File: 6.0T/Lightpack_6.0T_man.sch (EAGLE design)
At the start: 31 parts, among them CN1 USB-MICRO-B, CN2 RJ11-5P-REEL-LIGHTPACK6T2, CN3 RJ11-5P-REEL-MAIN, IC1 AT90USB162, IC2 DM631_SOP24, IC3 DM631_SOP24, J1 DCJ0202, X1 16Mhz

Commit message: New universal microUSB footprint
*Some restriction added
*7 holes on milling (46) layer
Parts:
- CN1: value USB-MICRO-B -> USB-MICRO-B-UNIVERSAL; device _USB_sockets:USB-MICRO-B -> _USB_sockets:USB-MICRO-B-UNIVERSAL
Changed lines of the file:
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@@
 <grid distance="0.1" unitdist="inch" unit="inch" style="lines" multiple="1" display="no" altdistance="0.01" altunitdist="inch" altunit="inch"/>
 <layers>
-<layer number="1" name="Top" color="4" fill="1" visible="no" active="no"/>
-<layer number="2" name="Route2" color="1" fill="3" visible="no" active="no"/>
-<layer number="15" name="Route15" color="4" fill="6" visible="no" active="no"/>
-<layer number="16" name="Bottom" color="1" fill="1" visible="no" active="no"/>
-<layer number="17" name="Pads" color="2" fill="1" visible="no" active="no"/>
-<layer number="18" name="Vias" color="2" fill="1" visible="no" active="no"/>
-<layer number="19" name="Unrouted" color="6" fill="1" visible="no" active="no"/>
-<layer number="20" name="Dimension" color="15" fill="1" visible="no" active="no"/>
-<layer number="21" name="tPlace" color="14" fill="1" visible="no" active="no"/>
-<layer number="22" name="bPlace" color="7" fill="1" visible="no" active="no"/>
-<layer number="23" name="tOrigins" color="15" fill="1" visible="no" active="no"/>
-<layer number="24" name="bOrigins" color="15" fill="1" visible="no" active="no"/>
-<layer number="25" name="tNames" color="7" fill="1" visible="no" active="no"/>
-<layer number="26" name="bNames" color="7" fill="1" visible="no" active="no"/>
-<layer number="27" name="tValues" color="7" fill="1" visible="no" active="no"/>
-<layer number="28" name="bValues" color="7" fill="1" visible="no" active="no"/>
+<layer number="1" name="Top" color="4" fill="1" visible="yes" active="no"/>
+<layer number="2" name="Route2" color="1" fill="3" visible="yes" active="no"/>
+<layer number="15" name="Route15" color="4" fill="6" visible="yes" active="no"/>
+<layer number="16" name="Bottom" color="1" fill="1" visible="yes" active="no"/>
+<layer number="17" name="Pads" color="2" fill="1" visible="yes" active="no"/>
+<layer number="18" name="Vias" color="2" fill="1" visible="yes" active="no"/>
+<layer number="19" name="Unrouted" color="6" fill="1" visible="yes" active="no"/>
+<layer number="20" name="Dimension" color="15" fill="1" visible="yes" active="no"/>
+<layer number="21" name="tPlace" color="14" fill="1" visible="yes" active="no"/>
+<layer number="22" name="bPlace" color="7" fill="1" visible="yes" active="no"/>
+<layer number="23" name="tOrigins" color="15" fill="1" visible="yes" active="no"/>
+<layer number="24" name="bOrigins" color="15" fill="1" visible="yes" active="no"/>
+<layer number="25" name="tNames" color="7" fill="1" visible="yes" active="no"/>
+<layer number="26" name="bNames" color="7" fill="1" visible="yes" active="no"/>
+<layer number="27" name="tValues" color="7" fill="1" visible="yes" active="no"/>
+<layer number="28" name="bValues" color="7" fill="1" visible="yes" active="no"/>
 <layer number="29" name="tStop" color="7" fill="3" visible="no" active="no"/>
 <layer number="30" name="bStop" color="7" fill="6" visible="no" active="no"/>
@@
 <layer number="35" name="tGlue" color="7" fill="4" visible="no" active="no"/>
 <layer number="36" name="bGlue" color="7" fill="5" visible="no" active="no"/>
-<layer number="37" name="tTest" color="7" fill="1" visible="no" active="no"/>
-<layer number="38" name="bTest" color="7" fill="1" visible="no" active="no"/>
+<layer number="37" name="tTest" color="7" fill="1" visible="yes" active="no"/>
+<layer number="38" name="bTest" color="7" fill="1" visible="yes" active="no"/>
 <layer number="39" name="tKeepout" color="4" fill="11" visible="no" active="no"/>
 <layer number="40" name="bKeepout" color="1" fill="11" visible="no" active="no"/>
@@
 <layer number="44" name="Drills" color="7" fill="1" visible="no" active="no"/>
 <layer number="45" name="Holes" color="7" fill="1" visible="no" active="no"/>
-<layer number="46" name="Milling" color="3" fill="1" visible="no" active="no"/>
-<layer number="47" name="Measures" color="7" fill="1" visible="no" active="no"/>
-<layer number="48" name="Document" color="7" fill="1" visible="no" active="no"/>
-<layer number="49" name="Reference" color="7" fill="1" visible="no" active="no"/>
-<layer number="50" name="dxf" color="7" fill="1" visible="no" active="no"/>
-<layer number="51" name="tDocu" color="7" fill="1" visible="no" active="no"/>
-<layer number="52" name="bDocu" color="7" fill="1" visible="no" active="no"/>
-<layer number="53" name="tGND_GNDA" color="7" fill="9" visible="no" active="no"/>
-<layer number="54" name="bGND_GNDA" color="1" fill="9" visible="no" active="no"/>
-<layer number="56" name="wert" color="7" fill="1" visible="no" active="no"/>
+<layer number="46" name="Milling" color="3" fill="1" visible="yes" active="no"/>
+<layer number="47" name="Measures" color="7" fill="1" visible="yes" active="no"/>
+<layer number="48" name="Document" color="7" fill="1" visible="yes" active="no"/>
+<layer number="49" name="Reference" color="7" fill="1" visible="yes" active="no"/>
+<layer number="50" name="dxf" color="7" fill="1" visible="yes" active="no"/>
+<layer number="51" name="tDocu" color="7" fill="1" visible="yes" active="no"/>
+<layer number="52" name="bDocu" color="7" fill="1" visible="yes" active="no"/>
+<layer number="53" name="tGND_GNDA" color="7" fill="9" visible="yes" active="no"/>
+<layer number="54" name="bGND_GNDA" color="1" fill="9" visible="yes" active="no"/>
+<layer number="56" name="wert" color="7" fill="1" visible="yes" active="no"/>
 <layer number="91" name="Nets" color="2" fill="1" visible="yes" active="yes"/>
 <layer number="92" name="Busses" color="1" fill="1" visible="yes" active="yes"/>
@@
 <part name="GND11" library="supply1" deviceset="GND" device=""/>
 <part name="FRAME2" library="frames" deviceset="A4L-LOC" device="" value="Lightpack"/>
-<part name="CN1" library="_USB_sockets" deviceset="USB-MICRO-B" device=""/>
+<part name="CN1" library="_USB_sockets" deviceset="USB-MICRO-B" device="-UNIVERSAL"/>
 <part name="GND13" library="supply1" deviceset="GND" device=""/>
 <part name="C6" library="rcl" deviceset="C-EU" device="C0805" value="10nF/500V"/>

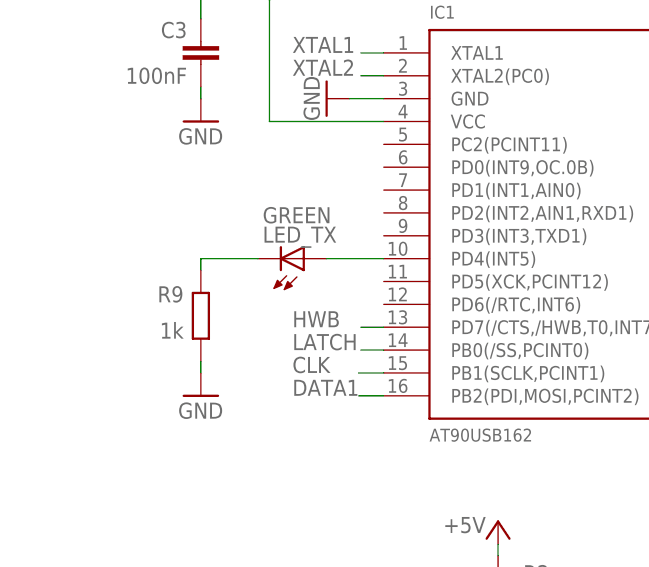
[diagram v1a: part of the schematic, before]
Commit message: Fix names and R9 value
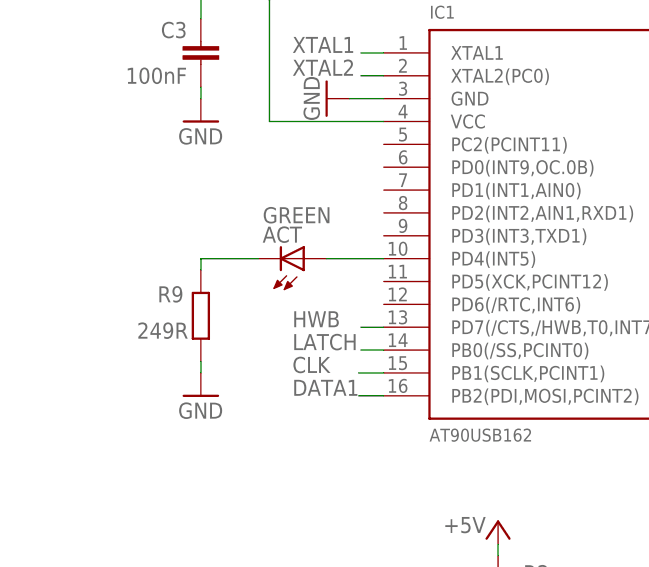
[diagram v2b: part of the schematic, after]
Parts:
- R9: value 1k -> 249R
- renumbered LED_TX to ACT
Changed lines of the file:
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@@
 <grid distance="0.1" unitdist="inch" unit="inch" style="lines" multiple="1" display="no" altdistance="0.01" altunitdist="inch" altunit="inch"/>
 <layers>
-<layer number="1" name="Top" color="4" fill="1" visible="yes" active="no"/>
-<layer number="2" name="Route2" color="1" fill="3" visible="yes" active="no"/>
-<layer number="15" name="Route15" color="4" fill="6" visible="yes" active="no"/>
-<layer number="16" name="Bottom" color="1" fill="1" visible="yes" active="no"/>
-<layer number="17" name="Pads" color="2" fill="1" visible="yes" active="no"/>
-<layer number="18" name="Vias" color="2" fill="1" visible="yes" active="no"/>
-<layer number="19" name="Unrouted" color="6" fill="1" visible="yes" active="no"/>
-<layer number="20" name="Dimension" color="15" fill="1" visible="yes" active="no"/>
-<layer number="21" name="tPlace" color="14" fill="1" visible="yes" active="no"/>
-<layer number="22" name="bPlace" color="7" fill="1" visible="yes" active="no"/>
-<layer number="23" name="tOrigins" color="15" fill="1" visible="yes" active="no"/>
-<layer number="24" name="bOrigins" color="15" fill="1" visible="yes" active="no"/>
-<layer number="25" name="tNames" color="7" fill="1" visible="yes" active="no"/>
-<layer number="26" name="bNames" color="7" fill="1" visible="yes" active="no"/>
-<layer number="27" name="tValues" color="7" fill="1" visible="yes" active="no"/>
-<layer number="28" name="bValues" color="7" fill="1" visible="yes" active="no"/>
+<layer number="1" name="Top" color="4" fill="1" visible="no" active="no"/>
+<layer number="2" name="Route2" color="1" fill="3" visible="no" active="no"/>
+<layer number="15" name="Route15" color="4" fill="6" visible="no" active="no"/>
+<layer number="16" name="Bottom" color="1" fill="1" visible="no" active="no"/>
+<layer number="17" name="Pads" color="2" fill="1" visible="no" active="no"/>
+<layer number="18" name="Vias" color="2" fill="1" visible="no" active="no"/>
+<layer number="19" name="Unrouted" color="6" fill="1" visible="no" active="no"/>
+<layer number="20" name="Dimension" color="15" fill="1" visible="no" active="no"/>
+<layer number="21" name="tPlace" color="14" fill="1" visible="no" active="no"/>
+<layer number="22" name="bPlace" color="7" fill="1" visible="no" active="no"/>
+<layer number="23" name="tOrigins" color="15" fill="1" visible="no" active="no"/>
+<layer number="24" name="bOrigins" color="15" fill="1" visible="no" active="no"/>
+<layer number="25" name="tNames" color="7" fill="1" visible="no" active="no"/>
+<layer number="26" name="bNames" color="7" fill="1" visible="no" active="no"/>
+<layer number="27" name="tValues" color="7" fill="1" visible="no" active="no"/>
+<layer number="28" name="bValues" color="7" fill="1" visible="no" active="no"/>
 <layer number="29" name="tStop" color="7" fill="3" visible="no" active="no"/>
 <layer number="30" name="bStop" color="7" fill="6" visible="no" active="no"/>
@@
 <layer number="35" name="tGlue" color="7" fill="4" visible="no" active="no"/>
 <layer number="36" name="bGlue" color="7" fill="5" visible="no" active="no"/>
-<layer number="37" name="tTest" color="7" fill="1" visible="yes" active="no"/>
-<layer number="38" name="bTest" color="7" fill="1" visible="yes" active="no"/>
+<layer number="37" name="tTest" color="7" fill="1" visible="no" active="no"/>
+<layer number="38" name="bTest" color="7" fill="1" visible="no" active="no"/>
 <layer number="39" name="tKeepout" color="4" fill="11" visible="no" active="no"/>
 <layer number="40" name="bKeepout" color="1" fill="11" visible="no" active="no"/>
@@
 <layer number="44" name="Drills" color="7" fill="1" visible="no" active="no"/>
 <layer number="45" name="Holes" color="7" fill="1" visible="no" active="no"/>
-<layer number="46" name="Milling" color="3" fill="1" visible="yes" active="no"/>
-<layer number="47" name="Measures" color="7" fill="1" visible="yes" active="no"/>
-<layer number="48" name="Document" color="7" fill="1" visible="yes" active="no"/>
-<layer number="49" name="Reference" color="7" fill="1" visible="yes" active="no"/>
-<layer number="50" name="dxf" color="7" fill="1" visible="yes" active="no"/>
-<layer number="51" name="tDocu" color="7" fill="1" visible="yes" active="no"/>
-<layer number="52" name="bDocu" color="7" fill="1" visible="yes" active="no"/>
-<layer number="53" name="tGND_GNDA" color="7" fill="9" visible="yes" active="no"/>
-<layer number="54" name="bGND_GNDA" color="1" fill="9" visible="yes" active="no"/>
-<layer number="56" name="wert" color="7" fill="1" visible="yes" active="no"/>
+<layer number="46" name="Milling" color="3" fill="1" visible="no" active="no"/>
+<layer number="47" name="Measures" color="7" fill="1" visible="no" active="no"/>
+<layer number="48" name="Document" color="7" fill="1" visible="no" active="no"/>
+<layer number="49" name="Reference" color="7" fill="1" visible="no" active="no"/>
+<layer number="50" name="dxf" color="7" fill="1" visible="no" active="no"/>
+<layer number="51" name="tDocu" color="7" fill="1" visible="no" active="no"/>
+<layer number="52" name="bDocu" color="7" fill="1" visible="no" active="no"/>
+<layer number="53" name="tGND_GNDA" color="7" fill="9" visible="no" active="no"/>
+<layer number="54" name="bGND_GNDA" color="1" fill="9" visible="no" active="no"/>
+<layer number="56" name="wert" color="7" fill="1" visible="no" active="no"/>
 <layer number="91" name="Nets" color="2" fill="1" visible="yes" active="yes"/>
 <layer number="92" name="Busses" color="1" fill="1" visible="yes" active="yes"/>
@@
 <part name="D2" library="diode" deviceset="DIODE-" device="SMB" value="SS14"/>
 <part name="GND9" library="supply1" deviceset="GND" device=""/>
-<part name="LED_TX" library="adafruit" deviceset="LED" device="3MM" value="GREEN"/>
+<part name="ACT" library="adafruit" deviceset="LED" device="3MM" value="GREEN"/>
 <part name="GND19" library="supply1" deviceset="GND" device=""/>
-<part name="R9" library="rcl" deviceset="R-EU_" device="R0805" value="1k"/>
+<part name="R9" library="rcl" deviceset="R-EU_" device="R0805" value="249R"/>
 <part name="C3" library="rcl" deviceset="C-EU" device="C0805" value="100nF"/>
 <part name="GND20" library="supply1" deviceset="GND" device=""/>
@@
 <instance part="D2" gate="G$1" x="232.41" y="167.64"/>
 <instance part="GND9" gate="1" x="66.04" y="123.19"/>
-<instance part="LED_TX" gate="G$1" x="36.83" y="80.01" rot="MR90"/>
+<instance part="ACT" gate="G$1" x="36.83" y="80.01" rot="MR90"/>
 <instance part="GND19" gate="1" x="25.4" y="64.77"/>
 <instance part="R9" gate="G$1" x="25.4" y="73.66" smashed="yes" rot="R90">
 <attribute name="NAME" x="20.574" y="75.1586" size="1.778" layer="95"/>
-<attribute name="VALUE" x="20.828" y="71.12" size="1.778" layer="96"/>
+<attribute name="VALUE" x="18.288" y="71.12" size="1.778" layer="96"/>
 </instance>
 <instance part="C3" gate="G$1" x="25.4" y="104.14" rot="MR0"/>
@@
 <wire x1="25.4" y1="78.74" x2="25.4" y2="80.01" width="0.1524" layer="91"/>
 <pinref part="R9" gate="G$1" pin="2"/>
-<pinref part="LED_TX" gate="G$1" pin="C"/>
+<pinref part="ACT" gate="G$1" pin="C"/>
 <wire x1="31.75" y1="80.01" x2="25.4" y2="80.01" width="0.2032" layer="91"/>
 </segment>
@@
 <net name="N$3" class="0">
 <segment>
-<pinref part="LED_TX" gate="G$1" pin="A"/>
+<pinref part="ACT" gate="G$1" pin="A"/>
 <pinref part="IC1" gate="G$1" pin="PD4(INT5)"/>
 <wire x1="39.37" y1="80.01" x2="45.72" y2="80.01" width="0.2032" layer="91"/>

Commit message: tSilk + new microUSB socket + CN2,CN3 moving (see details)
-- P/N + ID on tSilk
-- Slots of mUSB increased to 1.0x0.5mm
-- New solid rect in mUSB component (commited in Pixelkit lib) named EVT
-- CN2,3 moved on 0.1mm out of center
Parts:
- CN1: value USB-MICRO-B-UNIVERSAL -> USB-MICRO-B-EVT; device _USB_sockets:USB-MICRO-B-UNIVERSAL -> _USB_sockets:USB-MICRO-B-EVT
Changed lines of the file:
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@@
 <part name="GND11" library="supply1" deviceset="GND" device=""/>
 <part name="FRAME2" library="frames" deviceset="A4L-LOC" device="" value="Lightpack"/>
-<part name="CN1" library="_USB_sockets" deviceset="USB-MICRO-B" device="-UNIVERSAL"/>
+<part name="CN1" library="_USB_sockets" deviceset="USB-MICRO-B" device="-EVT"/>
 <part name="GND13" library="supply1" deviceset="GND" device=""/>
 <part name="C6" library="rcl" deviceset="C-EU" device="C0805" value="10nF/500V"/>
